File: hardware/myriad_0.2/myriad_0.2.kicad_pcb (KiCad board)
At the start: 4 copper layers, 61 x 108 mm, 108 parts, among them J1 CV In 1, J10 ELI2040B 1, J2 CV In 2, J3 ELI2040B 1, J4 CV In 3, J5 CV In 4, J6 Clean Out, J7 Shaped Out, J8 Conn_01x02_Socket, J9 Conn_01x02_Socket, Q1 MMBT3906, Q2 MMBT3904, Q3 MMBT3906, Q4 MMBT3904, SW1 TS-1187A-B-A-B, U1 TL072, U2 MCP6002-xMS, U3 CJ431 SOT-23, U4 CJ431 SOT-23, U5 TL072, U6 TL072, U7 MCP6002-xMS, U8 TL072

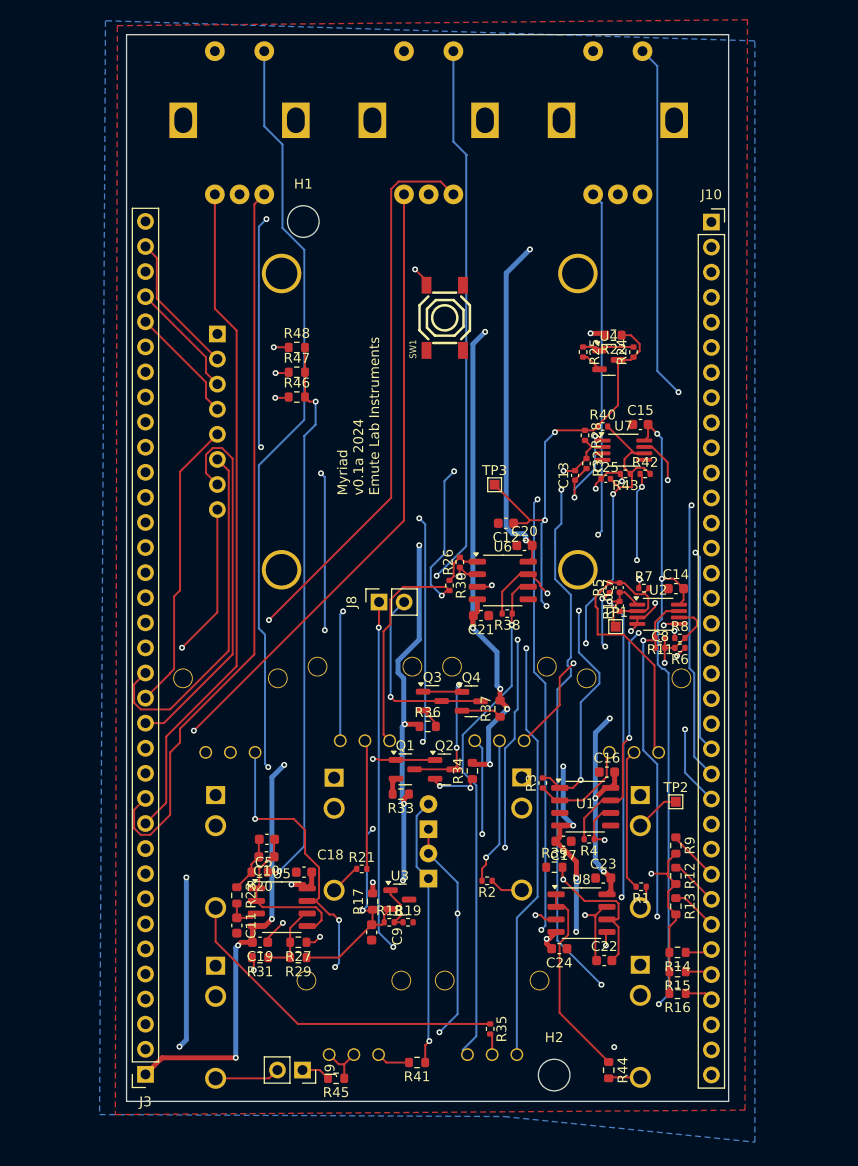
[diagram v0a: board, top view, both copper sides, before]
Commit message: finally approaching multiple pitch control
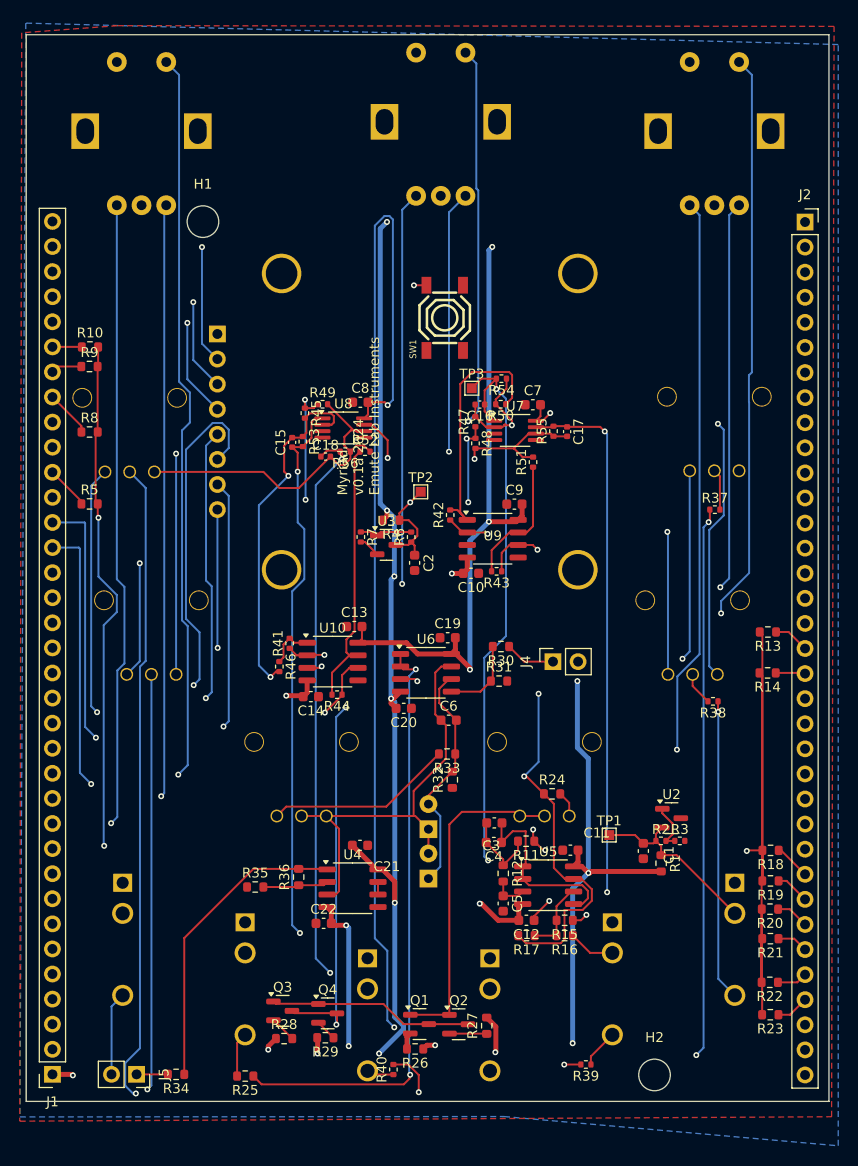
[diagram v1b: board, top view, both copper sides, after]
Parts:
- added C21: 100n, Capacitor_SMD:C_0603_1608Metric, F.Cu at (188.6, 119.8)
- added C22: 100n, Capacitor_SMD:C_0603_1608Metric, F.Cu at (184.9, 127.7)
- added R13: 33k, Resistor_SMD:R_0603_1608Metric, F.Cu at (229.9, 98.2)
- added R14: 33k, Resistor_SMD:R_0603_1608Metric, F.Cu at (229.9, 102.3)
- added R24: 10k, Resistor_SMD:R_0603_1608Metric, F.Cu at (208.1, 114.6)
- added R30: 10k, Resistor_SMD:R_0603_1608Metric, F.Cu at (202.9, 99.7)
- added R31: 5k, Resistor_SMD:R_0603_1608Metric, F.Cu at (202.7, 103.2)
- added R35: 10k, Resistor_SMD:R_0603_1608Metric, F.Cu at (178.0, 124.0)
- added R36: 38k, Resistor_SMD:R_0603_1608Metric, F.Cu at (182.4, 123.0)
- added R8: 33k, Resistor_SMD:R_0603_1608Metric, F.Cu at (161.2, 78.0)
- added U4: TL072, Package_SO:SO-8_3.9x4.9mm_P1.27mm, F.Cu at (187.9, 124.2)
- R11: renamed from R20; value 1.3k -> 1.2k
- R12: renamed from R23; value 1.3k -> 1.2k
- R33: renamed from R41; value 560 -> 2k
- moved RV4 69.5 mm to (165.3, 74.5)
- moved R37 51.0 mm to (224.6, 85.8)
- moved RV1 44.7 mm to (224.5, 74.4)
- moved J3 40.2 mm to (177.0, 127.6)
- moved R29 37.7 mm to (185.1, 139.3), turned to 180 degrees
- moved R25 36.8 mm to (177.0, 143.2), turned to 180 degrees
- moved RV3 35.9 mm to (167.5, 95.0)
- moved Q3 34.8 mm to (180.8, 136.6)
- moved Q4 34.8 mm to (185.3, 136.8)
- moved R28 34.8 mm to (180.9, 139.4)
- moved RV4_Waveshape1 32.4 mm to (207.3, 109.3)
- moved R33 31.4 mm to (197.4, 110.6)
- moved R1 29.5 mm to (219.1, 121.6), turned to -90 degrees
- moved R7 29.3 mm to (188.7, 88.6)
- moved R4 29.3 mm to (191.8, 86.9)
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- renumbered C9 to C1, C17 to C10, C18 to C11, C19 to C12, C20 to C13, C21 to C14, C13 to C15, C7 to C16, C8 to C17, C25 to C18, C23 to C19, C12 to C2, C24 to C20, C5 to C3, C10 to C4, C11 to C5, C22 to C6, C14 to C7, C15 to C8, C16 to C9, D3 to D1, D4 to D2, J3 to J1, J5 to J10, J10 to J2, J6 to J3, J8 to J4, J9 to J5, J7 to J6, J4 to J7, J1 to J8, J2 to J9, R17 to R1, R48 to R10, R27 to R15, R29 to R16, R31 to R17, R9 to R18, R12 to R19, R18 to R2, R13 to R20, R14 to R21, R15 to R22, R16 to R23, R44 to R25, R33 to R26, R34 to R27, R36 to R28, R37 to R29, R19 to R3, R39 to R32, R45 to R34, R21 to R37, R1 to R38, R2 to R39, R22 to R4, R35 to R40, R26 to R41, R3 to R42, R4 to R43, R38 to R44, R28 to R45, R30 to R46, R5 to R47, R6 to R48, R40 to R49, R46 to R5, R7 to R50, R8 to R51, R42 to R52, R32 to R53, R10 to R54, R11 to R55, R43 to R56, R24 to R6, R25 to R7, R47 to R9, RV3 to RV1, RV1 to RV2, RV2 to RV3, RV5 to RV4, RV4 to RV4_Waveshape1, RV6 to RV6_Overdrive1, S2 to S1, S3 to S2, S1 to S3, TP2 to TP1, TP3 to TP2, TP1 to TP3, U9 to U1, U6 to U10, U3 to U2, U4 to U3, U8 to U6, U2 to U7, U7 to U8, U1 to U9
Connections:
- C6 pad 1: Net-(D3-A) -> Net-(D1-A)
- D1 pad 2: Net-(D3-A) -> Net-(D1-A)
- D2 pad 1: Net-(D3-A) -> Net-(D1-A)
- J1 pad 22: Net-(J10-Pin_22) -> Net-(J1-Pin_22)
- J1 pad 23: Net-(J10-Pin_24) -> Net-(J1-Pin_23)
- J1 pad 24: Net-(J10-Pin_23) -> unconnected-(J1-Pin_24-Pad24)
- J1 pad 25: Net-(J10-Pin_25) -> Net-(J1-Pin_25)
- J1 pad 28: Net-(J3-Pin_28) -> Net-(J1-Pin_28)
- J1 pad 4: GND -> unconnected-(J1-Pin_4-Pad4)
- J2 pad 1: unconnected-(J10--12V-Pad1) -> -12V
- J2 pad 18: unconnected-(J10-Pin_18-Pad18) -> Net-(J2-Pin_18)
- J2 pad 19: unconnected-(J10-Pin_19-Pad19) -> Net-(J2-Pin_19)
- J2 pad 22: Net-(J10-Pin_22) -> Net-(J1-Pin_23)
- J2 pad 23: Net-(J10-Pin_23) -> Net-(J1-Pin_22)
- J2 pad 24: Net-(J10-Pin_24) -> unconnected-(J2-Pin_24-Pad24)
- J2 pad 25: Net-(J10-Pin_25) -> unconnected-(J2-Pin_25-Pad25)
- J2 pad 4: GND -> unconnected-(J2-Pin_4-Pad4)
- J4 pad 1: Net-(J8-Pin_1) -> Net-(J4-Pin_1)
- R17 pad 2: Net-(U8A-+) -> Net-(U6A-+)
- R33 pad 2: Net-(R41-Pad2) (its old number) -> Net-(R33-Pad2)
- R34 pad 1: Net-(D3-A) -> Net-(R34-Pad1)
- R5 pad 1: Net-(J3-Pin_28) -> Net-(J1-Pin_25)
- RV4_Waveshape1 pad 1: Net-(U8A-+) -> Net-(R24-Pad2)
- RV4_Waveshape1 pad 3: GND -> Net-(Q1-B)
- RV6_Overdrive1 pad 1: Net-(R41-Pad2) (its old number) -> Net-(D1-A)
- RV6_Overdrive1 pad 2: Net-(D3-A) -> Net-(D1-A)
- RV6_Overdrive1 pad 3: Net-(D3-A) -> Net-(R33-Pad2)
- U5 pad 7: Net-(U8A-+) -> Net-(U6A-+)
- U6 pad 3: Net-(U8A-+) -> Net-(U6A-+)
- U6 pad 5: Net-(J8-Pin_1) -> Net-(U6B-+)
- U6 pad 7: Net-(D3-A) -> Net-(D1-A)
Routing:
- net Net-(J1-Pin_22): track 0.00 -> 99.8 mm, vias 0 -> 1
- net Net-(J1-Pin_23): track 0.00 -> 98.5 mm, vias 0 -> 1
- net Net-(J10-Pin_25): track 98.3 -> 0.00 mm, vias 4 -> 0
- net Net-(R40-Pad2): track 2.17 -> 98.7 mm, vias 0 -> 2
- net Net-(J10-Pin_24): track 86.1 -> 0.00 mm, vias 3 -> 0
- net Net-(R10-Pad2): track 112.4 -> 196.9 mm, vias 3 -> 5
- net Net-(J10-Pin_23): track 83.8 -> 0.00 mm, vias 1 -> 0
- net Net-(J10-Pin_22): track 78.0 -> 0.00 mm, vias 1 -> 0
- net Net-(J7-PadT): track 3.18 -> 77.4 mm, vias 0 -> 2
- net Net-(R39-Pad2): track 14.9 -> 87.1 mm, vias 1 -> 2
- net -12V: track 160.5 -> 230.3 mm, vias 15 -> 12
- net Net-(U8A-+): track 61.2 -> 0.00 mm, vias 5 -> 0
- net Net-(J8-Pin_1): track 58.6 -> 0.00 mm, vias 3 -> 0
- net Net-(D3-A): track 57.5 -> 0.00 mm, vias 3 -> 0
- net Net-(U8B--): track 90.3 -> 33.5 mm, vias 4 -> 0
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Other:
- board size 61 x 108 mm -> 81.3 x 108 mm
